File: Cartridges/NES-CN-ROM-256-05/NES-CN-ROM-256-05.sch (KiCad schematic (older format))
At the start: 14 parts, among them J1 32x8, J2 16x8

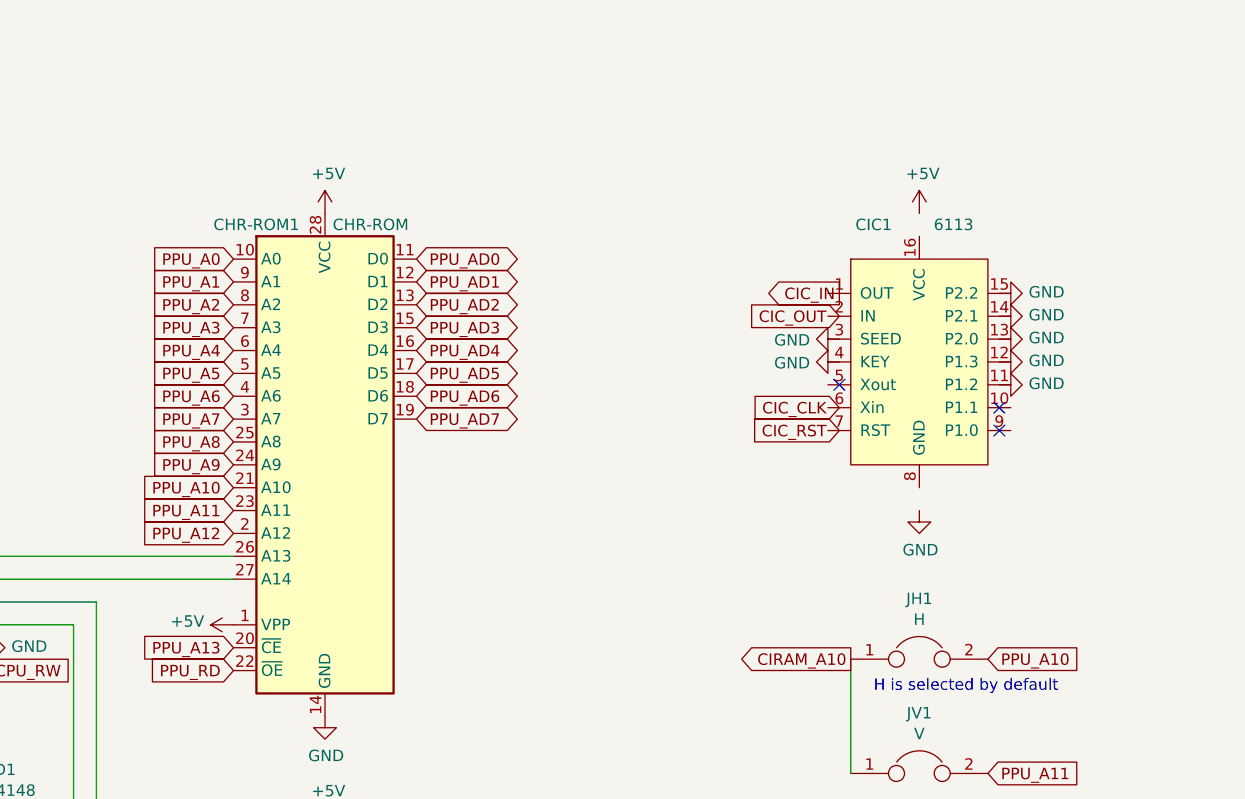
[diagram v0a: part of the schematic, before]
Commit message: Fix library components.
Change CHR-ROM library on MH and CN carts.
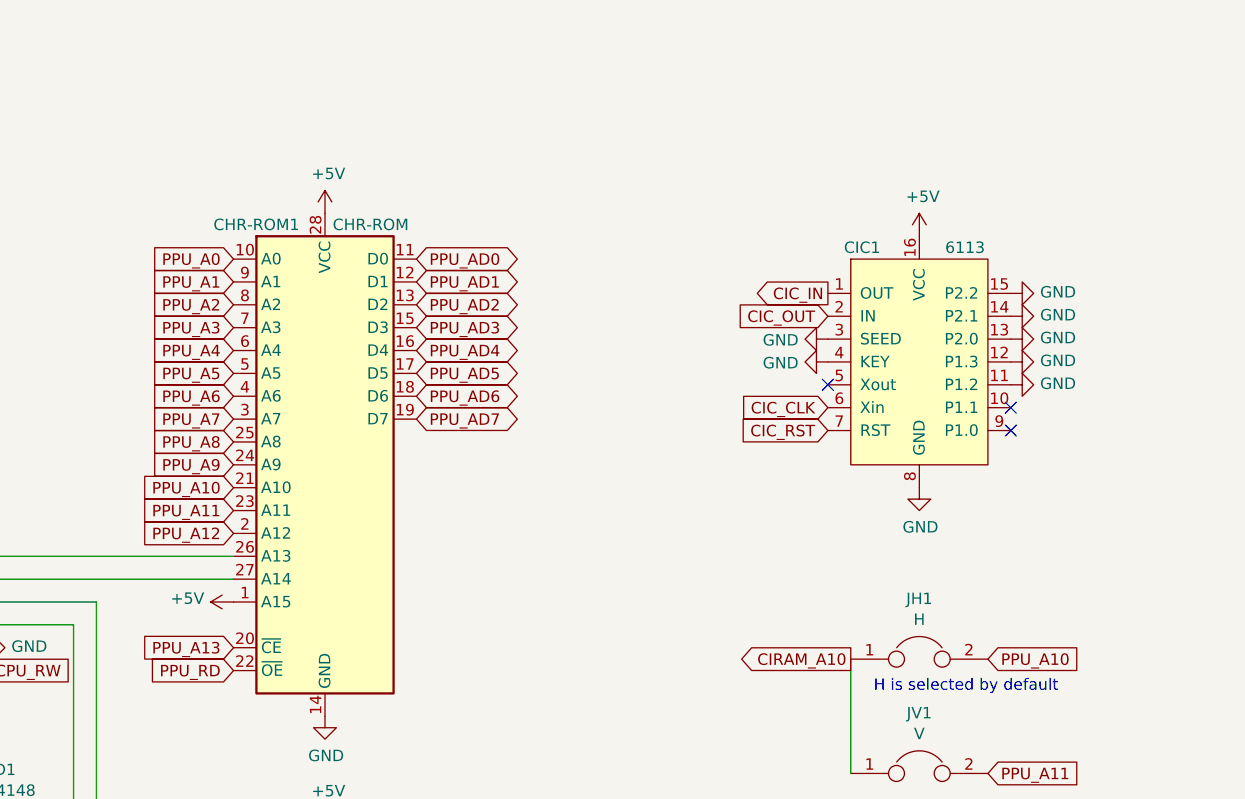
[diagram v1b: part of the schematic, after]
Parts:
- removed CHR-ROM1: CHR-ROM, Package_DIP:DIP-28_W15.24mm, symbol Memory_EPROM:27C256
- added CHR-ROM1: CHR-ROM, Package_DIP:DIP-28_W15.24mm, symbol Memory_EPROM:27C512
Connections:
- net +5V: now also CIC1.16 (VCC), CHR-ROM1.1 (A15), CHR-ROM1.28 (VCC)
- net CIC_CLK: now also CIC1.6 (Xin)
- net CIC_IN: now also CIC1.1 (OUT)
- net CIC_OUT: now also CIC1.2 (IN)
- net CIC_RST: now also CIC1.7 (RST)
- net GND: now also CIC1.11 (P1.2), CIC1.12 (P1.3), CIC1.13 (P2.0), CIC1.14 (P2.1), CIC1.15 (P2.2), CIC1.3 (SEED), CIC1.4 (KEY), CIC1.8 (GND), CHR-ROM1.14 (GND)
- net PPU_A0: now also CHR-ROM1.10 (A0)
- net PPU_A1: now also CHR-ROM1.9 (A1)
- net PPU_A10: now also CHR-ROM1.21 (A10)
- net PPU_A11: now also CHR-ROM1.23 (A11)
- net PPU_A12: now also CHR-ROM1.2 (A12)
- net PPU_A13: now also CHR-ROM1.20 (~CE)
- net PPU_A2: now also CHR-ROM1.8 (A2)
- net PPU_A3: now also CHR-ROM1.7 (A3)
- net PPU_A4: now also CHR-ROM1.6 (A4)
- net PPU_A5: now also CHR-ROM1.5 (A5)
- net PPU_A6: now also CHR-ROM1.4 (A6)
- net PPU_A7: now also CHR-ROM1.3 (A7)
- net PPU_A8: now also CHR-ROM1.25 (A8)
- net PPU_A9: now also CHR-ROM1.24 (A9)
- net PPU_AD0: now also CHR-ROM1.11 (D0)
- net PPU_AD1: now also CHR-ROM1.12 (D1)
- net PPU_AD2: now also CHR-ROM1.13 (D2)
- net PPU_AD3: now also CHR-ROM1.15 (D3)
- net PPU_AD4: now also CHR-ROM1.16 (D4)
- net PPU_AD5: now also CHR-ROM1.17 (D5)
- net PPU_AD6: now also CHR-ROM1.18 (D6)
- net PPU_AD7: now also CHR-ROM1.19 (D7)
- net PPU_RD: now also CHR-ROM1.22 (~OE)
- net at LS161.13 (Q1): now also CHR-ROM1.27 (A14)
- net at LS161.14 (Q0): now also CHR-ROM1.26 (A13)
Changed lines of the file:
@@
 U 1 1 5EDCEFFF
 P 6900 2100
-F 0 "CIC1" H 6700 2700 50  0000 C CNN
-F 1 "6113" H 7050 2700 50  0000 C CNN
+F 0 "CIC1" H 6650 2600 50  0000 C CNN
+F 1 "6113" H 7100 2600 50  0000 C CNN
 F 2 "Package_DIP:DIP-16_W7.62mm" V 6900 2100 50  0001 C CNN
 F 3 "" H 6900 1900 50  0001 C CNN
@@
 L power:GND #PWR0108
 U 1 1 5EDDE142
-P 6900 2750
-F 0 "#PWR0108" H 6900 2500 50  0001 C CNN
-F 1 "GND" H 6905 2577 50  0000 C CNN
-F 2 "" H 6900 2750 50  0001 C CNN
-F 3 "" H 6900 2750 50  0001 C CNN
-	1    6900 2750
+P 6900 2650
+F 0 "#PWR0108" H 6900 2400 50  0001 C CNN
+F 1 "GND" H 6905 2477 50  0000 C CNN
+F 2 "" H 6900 2650 50  0001 C CNN
+F 3 "" H 6900 2650 50  0001 C CNN
+	1    6900 2650
 	1    0    0    -1
 $EndComp
@@
 L power:+5V #PWR0109
 U 1 1 5EDDE4AD
-P 6900 1450
-F 0 "#PWR0109" H 6900 1300 50  0001 C CNN
-F 1 "+5V" H 6915 1623 50  0000 C CNN
-F 2 "" H 6900 1450 50  0001 C CNN
-F 3 "" H 6900 1450 50  0001 C CNN
-	1    6900 1450
+P 6900 1550
+F 0 "#PWR0109" H 6900 1400 50  0001 C CNN
+F 1 "+5V" H 6915 1723 50  0000 C CNN
+F 2 "" H 6900 1550 50  0001 C CNN
+F 3 "" H 6900 1550 50  0001 C CNN
+	1    6900 1550
 	1    0    0    -1
 $EndComp
@@
 L power:GND #PWR0116
 U 1 1 5EDECD9E
-P 6550 2000
-F 0 "#PWR0116" H 6550 1750 50  0001 C CNN
-F 1 "GND" V 6555 1872 50  0000 R CNN
-F 2 "" H 6550 2000 50  0001 C CNN
-F 3 "" H 6550 2000 50  0001 C CNN
-	1    6550 2000
+P 6500 2000
+F 0 "#PWR0116" H 6500 1750 50  0001 C CNN
+F 1 "GND" V 6505 1872 50  0000 R CNN
+F 2 "" H 6500 2000 50  0001 C CNN
+F 3 "" H 6500 2000 50  0001 C CNN
+	1    6500 2000
 	0    1    1    0
 $EndComp
@@
 L power:GND #PWR0117
 U 1 1 5EDED3D4
-P 6550 2100
-F 0 "#PWR0117" H 6550 1850 50  0001 C CNN
-F 1 "GND" V 6555 1972 50  0000 R CNN
-F 2 "" H 6550 2100 50  0001 C CNN
-F 3 "" H 6550 2100 50  0001 C CNN
-	1    6550 2100
+P 6500 2100
+F 0 "#PWR0117" H 6500 1850 50  0001 C CNN
+F 1 "GND" V 6505 1972 50  0000 R CNN
+F 2 "" H 6500 2100 50  0001 C CNN
+F 3 "" H 6500 2100 50  0001 C CNN
+	1    6500 2100
 	0    1    1    0
 $EndComp
@@
 L power:GND #PWR0118
 U 1 1 5EDED5CD
-P 7250 2200
-F 0 "#PWR0118" H 7250 1950 50  0001 C CNN
-F 1 "GND" V 7255 2072 50  0000 R CNN
-F 2 "" H 7250 2200 50  0001 C CNN
-F 3 "" H 7250 2200 50  0001 C CNN
-	1    7250 2200
+P 7300 2200
+F 0 "#PWR0118" H 7300 1950 50  0001 C CNN
+F 1 "GND" V 7305 2072 50  0000 R CNN
+F 2 "" H 7300 2200 50  0001 C CNN
+F 3 "" H 7300 2200 50  0001 C CNN
+	1    7300 2200
 	0    -1   -1   0
 $EndComp
@@
 L power:GND #PWR0119
 U 1 1 5EDEE169
-P 7250 2100
-F 0 "#PWR0119" H 7250 1850 50  0001 C CNN
-F 1 "GND" V 7255 1972 50  0000 R CNN
-F 2 "" H 7250 2100 50  0001 C CNN
-F 3 "" H 7250 2100 50  0001 C CNN
-	1    7250 2100
+P 7300 2100
+F 0 "#PWR0119" H 7300 1850 50  0001 C CNN
+F 1 "GND" V 7305 1972 50  0000 R CNN
+F 2 "" H 7300 2100 50  0001 C CNN
+F 3 "" H 7300 2100 50  0001 C CNN
+	1    7300 2100
 	0    -1   -1   0
 $EndComp
@@
 L power:GND #PWR0120
 U 1 1 5EDEE2B1
-P 7250 2000
-F 0 "#PWR0120" H 7250 1750 50  0001 C CNN
-F 1 "GND" V 7255 1872 50  0000 R CNN
-F 2 "" H 7250 2000 50  0001 C CNN
-F 3 "" H 7250 2000 50  0001 C CNN
-	1    7250 2000
+P 7300 2000
+F 0 "#PWR0120" H 7300 1750 50  0001 C CNN
+F 1 "GND" V 7305 1872 50  0000 R CNN
+F 2 "" H 7300 2000 50  0001 C CNN
+F 3 "" H 7300 2000 50  0001 C CNN
+	1    7300 2000
 	0    -1   -1   0
 $EndComp
@@
 L power:GND #PWR0121
 U 1 1 5EDEE59C
-P 7250 1900
-F 0 "#PWR0121" H 7250 1650 50  0001 C CNN
-F 1 "GND" V 7255 1772 50  0000 R CNN
-F 2 "" H 7250 1900 50  0001 C CNN
-F 3 "" H 7250 1900 50  0001 C CNN
-	1    7250 1900
+P 7300 1900
+F 0 "#PWR0121" H 7300 1650 50  0001 C CNN
+F 1 "GND" V 7305 1772 50  0000 R CNN
+F 2 "" H 7300 1900 50  0001 C CNN
+F 3 "" H 7300 1900 50  0001 C CNN
+	1    7300 1900
 	0    -1   -1   0
 $EndComp
@@
 L power:GND #PWR0122
 U 1 1 5EDEE777
-P 7250 1800
-F 0 "#PWR0122" H 7250 1550 50  0001 C CNN
-F 1 "GND" V 7255 1672 50  0000 R CNN
-F 2 "" H 7250 1800 50  0001 C CNN
-F 3 "" H 7250 1800 50  0001 C CNN
-	1    7250 1800
-	0    -1   -1   0
-$EndComp
-Text GLabel 6550 2300 0    50   Input ~ 0
+P 7300 1800
+F 0 "#PWR0122" H 7300 1550 50  0001 C CNN
+F 1 "GND" V 7305 1672 50  0000 R CNN
+F 2 "" H 7300 1800 50  0001 C CNN
+F 3 "" H 7300 1800 50  0001 C CNN
+	1    7300 1800
+	0    -1   -1   0
+$EndComp
+Text GLabel 6500 2300 0    50   Input ~ 0
 CIC_CLK
-Text GLabel 6550 2400 0    50   Input ~ 0
+Text GLabel 6500 2400 0    50   Input ~ 0
 CIC_RST
-Text GLabel 6550 1800 0    50   Output ~ 0
+Text GLabel 6500 1800 0    50   Output ~ 0
 CIC_IN
-Text GLabel 6550 1900 0    50   Input ~ 0
+Text GLabel 6500 1900 0    50   Input ~ 0
 CIC_OUT
-NoConn ~ 7250 2300
-NoConn ~ 7250 2400
-NoConn ~ 6550 2200
+NoConn ~ 7300 2300
+NoConn ~ 7300 2400
+NoConn ~ 6500 2200
 Text GLabel 3900 5050 0    50   Input ~ 0
 CPU_A7
@@
 Wire Wire Line
 	2800 2950 3900 2950
-$Comp
-L Memory_EPROM:27C256 CHR-ROM1
-U 1 1 5EE03E10
-P 4300 2550
-F 0 "CHR-ROM1" H 4000 3600 50  0000 C CNN
-F 1 "CHR-ROM" H 4500 3600 50  0000 C CNN
-F 2 "Package_DIP:DIP-28_W15.24mm" H 4300 2550 50  0001 C CNN
-F 3 "http://ww1.microchip.com/downloads/en/DeviceDoc/doc0014.pdf" H 4300 2550 50  0001 C CNN
-	1    4300 2550
-	1    0    0    -1
-$EndComp
 Wire Wire Line
 	2800 3050 3900 3050
@@
 L power:+5V #PWR0124
 U 1 1 5EDE512E
-P 3900 3250
-F 0 "#PWR0124" H 3900 3100 50  0001 C CNN
-F 1 "+5V" V 3915 3378 50  0000 L CNN
-F 2 "" H 3900 3250 50  0001 C CNN
-F 3 "" H 3900 3250 50  0001 C CNN
-	1    3900 3250
+P 3900 3150
+F 0 "#PWR0124" H 3900 3000 50  0001 C CNN
+F 1 "+5V" V 3915 3278 50  0000 L CNN
+F 2 "" H 3900 3150 50  0001 C CNN
+F 3 "" H 3900 3150 50  0001 C CNN
+	1    3900 3150
 	0    -1   -1   0
 $EndComp
@@
 Text GLabel 2750 4450 0    50   Output ~ 0
 PPU_A12
+$Comp
+L Memory_EPROM:27C512 CHR-ROM1
+U 1 1 5EE32C83
+P 4300 2550
+F 0 "CHR-ROM1" H 4000 3600 50  0000 C CNN
+F 1 "CHR-ROM" H 4500 3600 50  0000 C CNN
+F 2 "Package_DIP:DIP-28_W15.24mm" H 4300 2550 50  0001 C CNN
+F 3 "http://ww1.microchip.com/downloads/en/DeviceDoc/doc0015.pdf" H 4300 2550 50  0001 C CNN
+	1    4300 2550
+	1    0    0    -1
+$EndComp
 $EndSCHEMATC
